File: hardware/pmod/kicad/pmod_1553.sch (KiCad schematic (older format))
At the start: 30 parts, among them IC1 TB001-500-02BE, IC2 TB001-500-02BE, J1 Conn_02x06_Top_Bottom, J2 Conn_01x02, J3 Conn_01x02, P1 78604-9JC, P2 78604-9JC, U2 VO2630, U3 VO2630

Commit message: updated schematic with output filter caps on recieve line. Added AFRL logo as a library so it won't get deleted.
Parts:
- added C5, C6: 10pF, Capacitor_THT:C_Disc_D4.7mm_W2.5mm_P5.00mm, symbol Device:C
- added L1: afrl, logos:afrl, symbol logo:afrl
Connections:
- net GNDD: now also C5.1, C6.2
- net at J1.11 (Pin_11), R9.1, U3.6 (VO2): now also C5.2
- net at J1.9 (Pin_9), R10.2, U3.7 (VO1): now also C6.1
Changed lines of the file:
@@
 	6250 3050 6250 3350
 Connection ~ 6250 3350
+$Comp
+L Device:C C6
+U 1 1 6106DF8C
+P 5050 3600
+F 0 "C6" H 4875 3500 50  0000 L CNN
+F 1 "10pF" H 5100 3500 50  0000 L CNN
+F 2 "Capacitor_THT:C_Disc_D4.7mm_W2.5mm_P5.00mm" H 5088 3450 50  0001 C CNN
+F 3 "~" H 5050 3600 50  0001 C CNN
+	1    5050 3600
+	1    0    0    -1
+$EndComp
+Connection ~ 5050 3450
+$Comp
+L Device:C C5
+U 1 1 6106E50E
+P 4825 2950
+F 0 "C5" H 4625 2950 50  0000 L CNN
+F 1 "10pF" H 4925 2950 50  0000 L CNN
+F 2 "Capacitor_THT:C_Disc_D4.7mm_W2.5mm_P5.00mm" H 4863 2800 50  0001 C CNN
+F 3 "~" H 4825 2950 50  0001 C CNN
+	1    4825 2950
+	0    -1   -1   0
+$EndComp
+Connection ~ 4975 2950
+$Comp
+L power:GNDD #PWR06
+U 1 1 6106F8EA
+P 4675 2950
+F 0 "#PWR06" H 4675 2700 50  0001 C CNN
+F 1 "GNDD" H 4675 2800 50  0000 C CNN
+F 2 "" H 4675 2950 50  0001 C CNN
+F 3 "" H 4675 2950 50  0001 C CNN
+	1    4675 2950
+	0    1    1    0
+$EndComp
+$Comp
+L power:GNDD #PWR08
+U 1 1 6106FFF3
+P 5050 3750
+F 0 "#PWR08" H 5050 3500 50  0001 C CNN
+F 1 "GNDD" H 5050 3600 50  0000 C CNN
+F 2 "" H 5050 3750 50  0001 C CNN
+F 3 "" H 5050 3750 50  0001 C CNN
+	1    5050 3750
+	1    0    0    -1
+$EndComp
+$Comp
+L logo:afrl L1
+U 1 1 6108267E
+P 6050 6125
+F 0 "L1" H 6178 6171 50  0000 L CNN
+F 1 "afrl" H 6178 6080 50  0000 L CNN
+F 2 "logos:afrl" H 6050 6125 50  0001 C CNN
+F 3 "" H 6050 6125 50  0001 C CNN
+	1    6050 6125
+	1    0    0    -1
+$EndComp
 $EndSCHEMATC

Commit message: added testbench for fifos,they are barebones junk, but they are there and work with icarus.
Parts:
- C3, C4: value 22pF -> 10pF
- C5, C6: value 10pF -> 20pF
- R10, R9: value 2K2 -> 2K
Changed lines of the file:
@@
 P 6925 5225
 F 0 "C4" H 6700 5225 50  0000 L CNN
-F 1 "22pF" H 7050 5225 50  0000 L CNN
+F 1 "10pF" H 7050 5225 50  0000 L CNN
 F 2 "Capacitor_THT:C_Disc_D4.7mm_W2.5mm_P5.00mm" H 6963 5075 50  0001 C CNN
 F 3 "~" H 6925 5225 50  0001 C CNN
@@
 P 6925 4525
 F 0 "C3" H 6725 4525 50  0000 L CNN
-F 1 "22pF" H 7025 4525 50  0000 L CNN
+F 1 "10pF" H 7025 4525 50  0000 L CNN
 F 2 "Capacitor_THT:C_Disc_D4.7mm_W2.5mm_P5.00mm" H 6963 4375 50  0001 C CNN
 F 3 "~" H 6925 4525 50  0001 C CNN
@@
 P 5325 3500
 F 0 "R10" V 5118 3500 50  0000 C CNN
-F 1 "2K2" V 5209 3500 50  0000 C CNN
+F 1 "2K" V 5209 3500 50  0000 C CNN
 F 2 "Resistor_THT:R_Axial_DIN0207_L6.3mm_D2.5mm_P7.62mm_Horizontal" V 5255 3500 50  0001 C CNN
 F 3 "~" H 5325 3500 50  0001 C CNN
@@
 P 5325 2800
 F 0 "R9" V 5118 2800 50  0000 C CNN
-F 1 "2K2" V 5209 2800 50  0000 C CNN
+F 1 "2K" V 5209 2800 50  0000 C CNN
 F 2 "Resistor_THT:R_Axial_DIN0207_L6.3mm_D2.5mm_P7.62mm_Horizontal" V 5255 2800 50  0001 C CNN
 F 3 "~" H 5325 2800 50  0001 C CNN
@@
 P 5050 3600
 F 0 "C6" H 4875 3500 50  0000 L CNN
-F 1 "10pF" H 5100 3500 50  0000 L CNN
+F 1 "20pF" H 5100 3500 50  0000 L CNN
 F 2 "Capacitor_THT:C_Disc_D4.7mm_W2.5mm_P5.00mm" H 5088 3450 50  0001 C CNN
 F 3 "~" H 5050 3600 50  0001 C CNN
@@
 P 4825 2950
 F 0 "C5" H 4625 2950 50  0000 L CNN
-F 1 "10pF" H 4925 2950 50  0000 L CNN
+F 1 "20pF" H 4925 2950 50  0000 L CNN
 F 2 "Capacitor_THT:C_Disc_D4.7mm_W2.5mm_P5.00mm" H 4863 2800 50  0001 C CNN
 F 3 "~" H 4825 2950 50  0001 C CNN

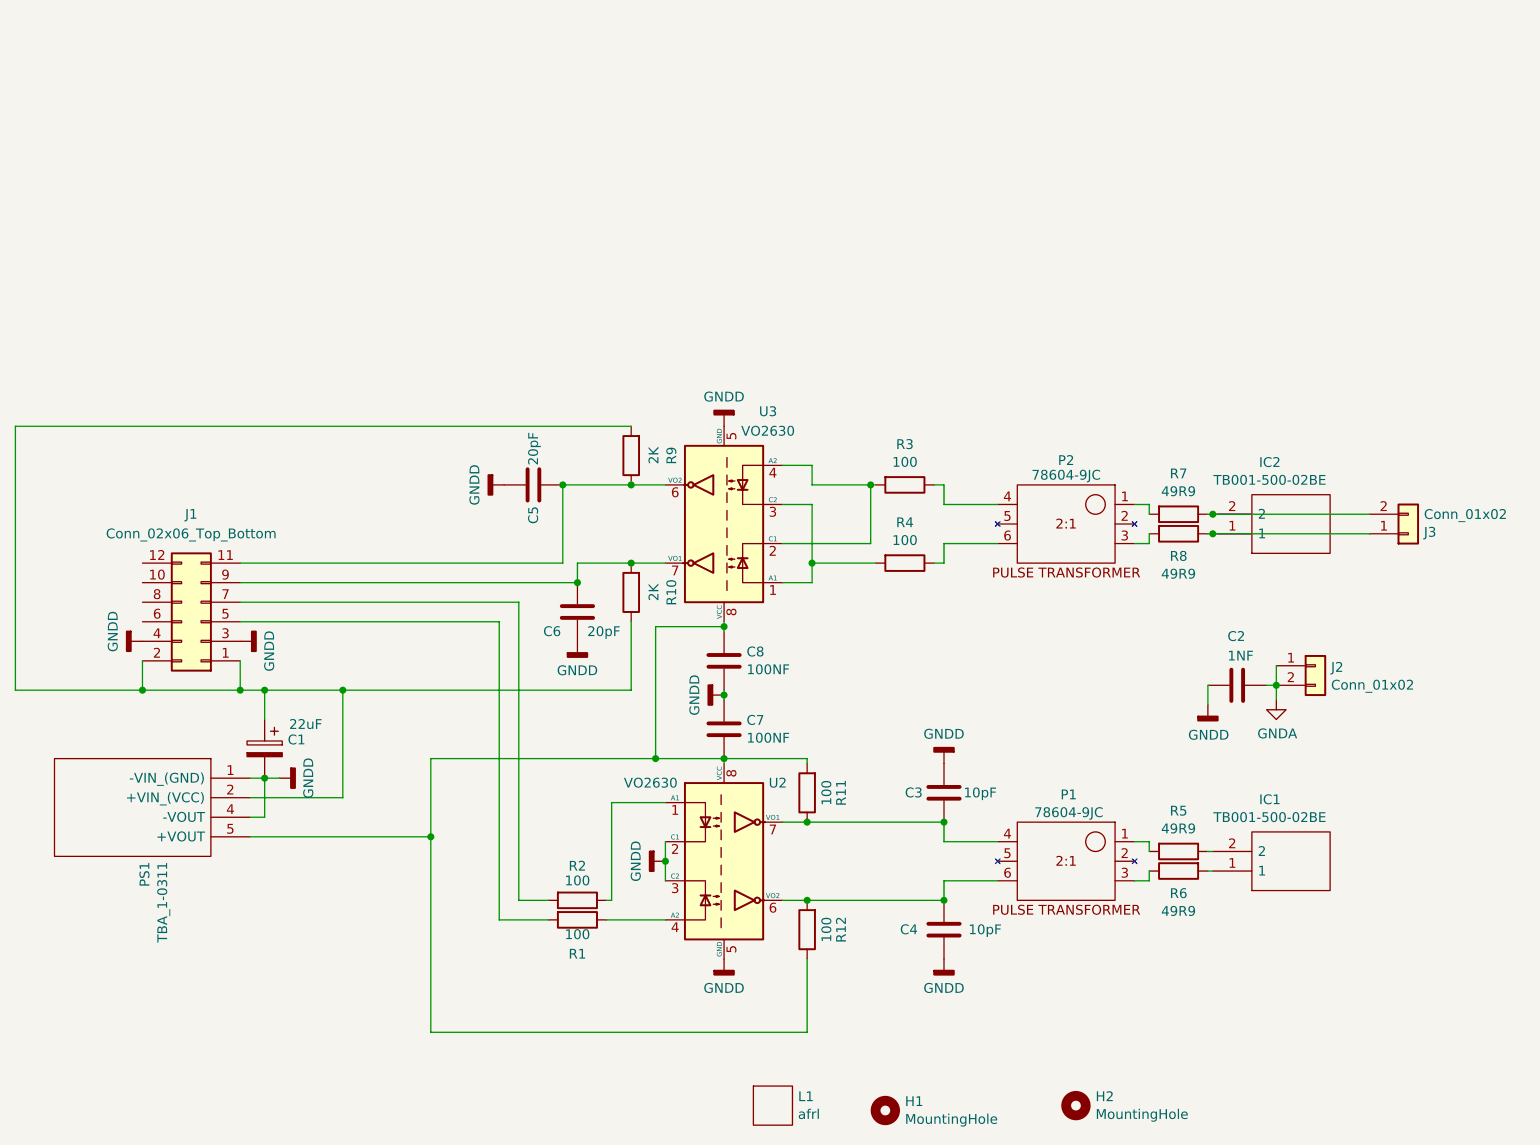
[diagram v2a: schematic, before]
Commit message: added 1553 to fmc1553 core, need adc/dac interface connection. added arty mcs file.
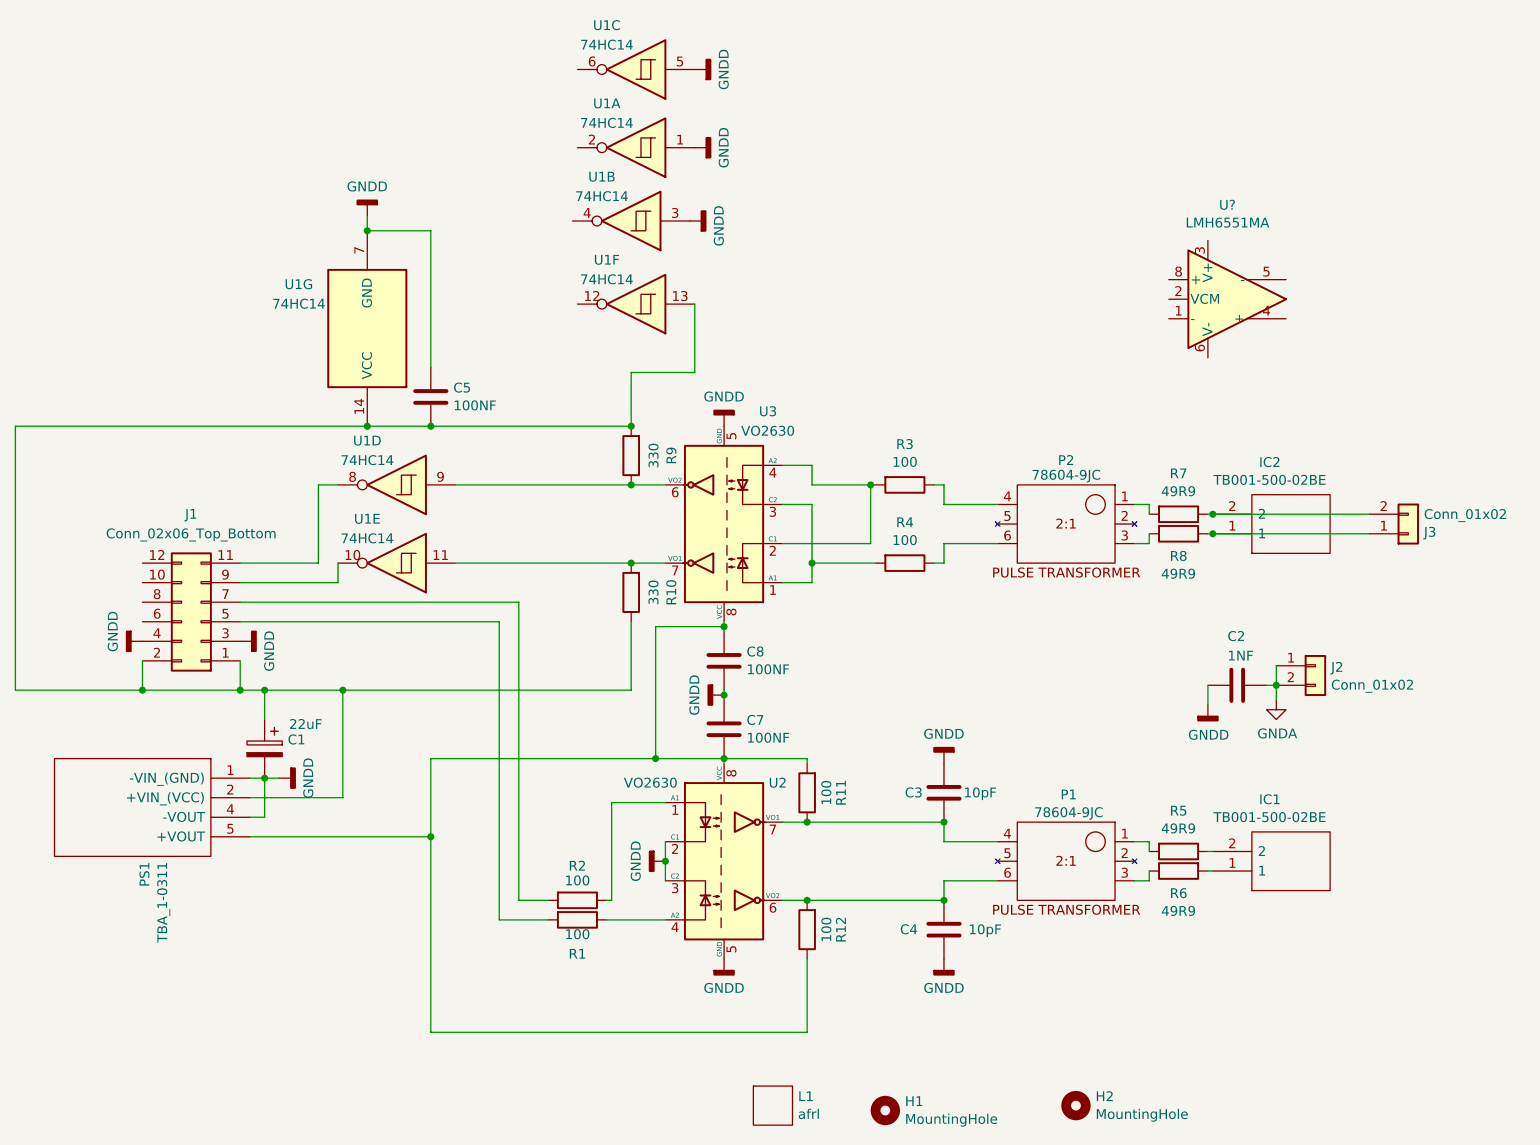
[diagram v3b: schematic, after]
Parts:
- removed C6: 20pF, Capacitor_THT:C_Disc_D4.7mm_W2.5mm_P5.00mm, symbol Device:C
- added U1: 74HC14, Package_DIP:DIP-14_W7.62mm_LongPads, symbol 74xx:74HC14
- added U?: LMH6551MA, Package_SO:SOIC-8_3.9x4.9mm_P1.27mm, symbol Amplifier_Operational:LMH6551MA
- C5: value 20pF -> 100NF
- R10, R9: value 2K -> 330
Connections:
- net GNDD: now also U1.1, U1.3, U1.5, U1.7 (GND)
- net at C1.1, J1.1 (Pin_1), J1.2 (Pin_2)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: now also C5.2, U1.13, U1.14 (VCC)
- net at R9.1, U3.6 (VO2): now also U1.9; no longer C5.2, J1.11 (Pin_11)
- net at R10.2, U3.7 (VO1): now also U1.11; no longer J1.9 (Pin_9)
- new net: J1.11 (Pin_11), U1.8
- new net: J1.9 (Pin_9), U1.10
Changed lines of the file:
@@
 $EndComp
-Wire Wire Line
-	3325 3450 5050 3450
-Wire Wire Line
-	5050 3450 5050 3350
-Wire Wire Line
-	4975 2950 4975 3350
-Wire Wire Line
-	4975 3350 3325 3350
-Wire Wire Line
-	4975 2950 5325 2950
 Wire Wire Line
 	3325 3650 4650 3650
@@
 P 5325 3500
 F 0 "R10" V 5118 3500 50  0000 C CNN
-F 1 "2K" V 5209 3500 50  0000 C CNN
+F 1 "330" V 5209 3500 50  0000 C CNN
 F 2 "Resistor_THT:R_Axial_DIN0207_L6.3mm_D2.5mm_P7.62mm_Horizontal" V 5255 3500 50  0001 C CNN
 F 3 "~" H 5325 3500 50  0001 C CNN
@@
 $EndComp
 Connection ~ 5325 3350
-Wire Wire Line
-	5325 3350 5050 3350
 $Comp
 L Device:R R9
@@
 P 5325 2800
 F 0 "R9" V 5118 2800 50  0000 C CNN
-F 1 "2K" V 5209 2800 50  0000 C CNN
+F 1 "330" V 5209 2800 50  0000 C CNN
 F 2 "Resistor_THT:R_Axial_DIN0207_L6.3mm_D2.5mm_P7.62mm_Horizontal" V 5255 2800 50  0001 C CNN
 F 3 "~" H 5325 2800 50  0001 C CNN
@@
 	2175 4000 2175 2650
 Wire Wire Line
-	2175 2650 5325 2650
+	2175 2650 3975 2650
 Connection ~ 2825 4000
 Wire Wire Line
@@
 Connection ~ 6250 3350
 $Comp
-L Device:C C6
-U 1 1 6106DF8C
-P 5050 3600
-F 0 "C6" H 4875 3500 50  0000 L CNN
-F 1 "20pF" H 5100 3500 50  0000 L CNN
-F 2 "Capacitor_THT:C_Disc_D4.7mm_W2.5mm_P5.00mm" H 5088 3450 50  0001 C CNN
-F 3 "~" H 5050 3600 50  0001 C CNN
-	1    5050 3600
-	1    0    0    -1
-$EndComp
-Connection ~ 5050 3450
-$Comp
-L Device:C C5
-U 1 1 6106E50E
-P 4825 2950
-F 0 "C5" H 4625 2950 50  0000 L CNN
-F 1 "20pF" H 4925 2950 50  0000 L CNN
-F 2 "Capacitor_THT:C_Disc_D4.7mm_W2.5mm_P5.00mm" H 4863 2800 50  0001 C CNN
-F 3 "~" H 4825 2950 50  0001 C CNN
-	1    4825 2950
-	0    -1   -1   0
-$EndComp
-Connection ~ 4975 2950
-$Comp
-L power:GNDD #PWR06
-U 1 1 6106F8EA
-P 4675 2950
-F 0 "#PWR06" H 4675 2700 50  0001 C CNN
-F 1 "GNDD" H 4675 2800 50  0000 C CNN
-F 2 "" H 4675 2950 50  0001 C CNN
-F 3 "" H 4675 2950 50  0001 C CNN
-	1    4675 2950
-	0    1    1    0
-$EndComp
-$Comp
-L power:GNDD #PWR08
-U 1 1 6106FFF3
-P 5050 3750
-F 0 "#PWR08" H 5050 3500 50  0001 C CNN
-F 1 "GNDD" H 5050 3600 50  0000 C CNN
-F 2 "" H 5050 3750 50  0001 C CNN
-F 3 "" H 5050 3750 50  0001 C CNN
-	1    5050 3750
-	1    0    0    -1
-$EndComp
-$Comp
 L logo:afrl L1
 U 1 1 6108267E
@@
 	1    0    0    -1
 $EndComp
+$Comp
+L 74xx:74HC14 U1
+U 1 1 6109BA4C
+P 5350 1225
+F 0 "U1" H 5500 1000 50  0000 C CNN
+F 1 "74HC14" H 5500 1100 50  0000 C CNN
+F 2 "Package_DIP:DIP-14_W7.62mm_LongPads" H 5350 1225 50  0001 C CNN
+F 3 "http://www.ti.com/lit/gpn/sn74HC14" H 5350 1225 50  0001 C CNN
+	1    5350 1225
+	-1   0    0    1
+$EndComp
+$Comp
+L 74xx:74HC14 U1
+U 2 1 610B023C
+P 5325 1600
+F 0 "U1" H 5475 1375 50  0000 C CNN
+F 1 "74HC14" H 5475 1475 50  0000 C CNN
+F 2 "Package_DIP:DIP-14_W7.62mm_LongPads" H 5325 1600 50  0001 C CNN
+F 3 "http://www.ti.com/lit/gpn/sn74HC14" H 5325 1600 50  0001 C CNN
+	2    5325 1600
+	-1   0    0    1
+$EndComp
+Wire Wire Line
+	4425 2950 5325 2950
+Wire Wire Line
+	4425 3350 5325 3350
+Wire Wire Line
+	3825 3450 3325 3450
+Wire Wire Line
+	3325 3350 3725 3350
+Wire Wire Line
+	3725 3350 3725 2950
+Wire Wire Line
+	3725 2950 3825 2950
+Wire Wire Line
+	3825 3350 3825 3450
+$Comp
+L 74xx:74HC14 U1
+U 7 1 610D764E
+P 3975 2150
+F 0 "U1" H 4325 1925 50  0000 C CNN
+F 1 "74HC14" H 4325 2025 50  0000 C CNN
+F 2 "Package_DIP:DIP-14_W7.62mm_LongPads" H 3975 2150 50  0001 C CNN
+F 3 "http://www.ti.com/lit/gpn/sn74HC14" H 3975 2150 50  0001 C CNN
+	7    3975 2150
+	-1   0    0    1
+$EndComp
+Connection ~ 3975 2650
+$Comp
+L power:GNDD #PWR06
+U 1 1 610E20D2
+P 3975 1575
+F 0 "#PWR06" H 3975 1325 50  0001 C CNN
+F 1 "GNDD" H 3975 1425 50  0000 C CNN
+F 2 "" H 3975 1575 50  0001 C CNN
+F 3 "" H 3975 1575 50  0001 C CNN
+	1    3975 1575
+	-1   0    0    1
+$EndComp
+$Comp
+L Device:C C5
+U 1 1 610E2A33
+P 4300 2500
+F 0 "C5" H 4415 2546 50  0000 L CNN
+F 1 "100NF" H 4415 2455 50  0000 L CNN
+F 2 "Capacitor_THT:C_Disc_D4.7mm_W2.5mm_P5.00mm" H 4338 2350 50  0001 C CNN
+F 3 "~" H 4300 2500 50  0001 C CNN
+	1    4300 2500
+	1    0    0    -1
+$EndComp
+Wire Wire Line
+	3975 1650 3975 1575
+Connection ~ 3975 1650
+Connection ~ 4300 2650
+Wire Wire Line
+	4300 2650 5325 2650
+Wire Wire Line
+	3975 2650 4300 2650
+Wire Wire Line
+	4300 2350 4300 1650
+Wire Wire Line
+	3975 1650 4300 1650
+$Comp
+L 74xx:74HC14 U1
+U 5 1 61103622
+P 4125 3350
+F 0 "U1" H 4275 3125 50  0000 C CNN
+F 1 "74HC14" H 4275 3225 50  0000 C CNN
+F 2 "" H 4125 3350 50  0001 C CNN
+F 3 "http://www.ti.com/lit/gpn/sn74HC14" H 4125 3350 50  0001 C CNN
+	5    4125 3350
+	-1   0    0    1
+$EndComp
+$Comp
+L 74xx:74HC14 U1
+U 6 1 61106EEA
+P 5350 2025
+F 0 "U1" H 5500 1800 50  0000 C CNN
+F 1 "74HC14" H 5500 1900 50  0000 C CNN
+F 2 "" H 5350 2025 50  0001 C CNN
+F 3 "http://www.ti.com/lit/gpn/sn74HC14" H 5350 2025 50  0001 C CNN
+	6    5350 2025
+	-1   0    0    1
+$EndComp
+$Comp
+L 74xx:74HC14 U1
+U 4 1 6110A8C5
+P 4125 2950
+F 0 "U1" H 4275 2725 50  0000 C CNN
+F 1 "74HC14" H 4275 2825 50  0000 C CNN
+F 2 "" H 4125 2950 50  0001 C CNN
+F 3 "http://www.ti.com/lit/gpn/sn74HC14" H 4125 2950 50  0001 C CNN
+	4    4125 2950
+	-1   0    0    1
+$EndComp
+$Comp
+L 74xx:74HC14 U1
+U 3 1 6110E653
+P 5350 825
+F 0 "U1" H 5500 600 50  0000 C CNN
+F 1 "74HC14" H 5500 700 50  0000 C CNN
+F 2 "" H 5350 825 50  0001 C CNN
+F 3 "http://www.ti.com/lit/gpn/sn74HC14" H 5350 825 50  0001 C CNN
+	3    5350 825
+	-1   0    0    1
+$EndComp
+$Comp
+L power:GNDD #PWR0105
+U 1 1 6111725A
+P 5625 1600
+F 0 "#PWR0105" H 5625 1350 50  0001 C CNN
+F 1 "GNDD" H 5600 1450 50  0000 C CNN
+F 2 "" H 5625 1600 50  0001 C CNN
+F 3 "" H 5625 1600 50  0001 C CNN
+	1    5625 1600
+	0    -1   -1   0
+$EndComp
+$Comp
+L power:GNDD #PWR0106
+U 1 1 6111F143
+P 5650 1225
+F 0 "#PWR0106" H 5650 975 50  0001 C CNN
+F 1 "GNDD" H 5650 1075 50  0000 C CNN
+F 2 "" H 5650 1225 50  0001 C CNN
+F 3 "" H 5650 1225 50  0001 C CNN
+	1    5650 1225
+	0    -1   -1   0
+$EndComp
+$Comp
+L power:GNDD #PWR0107
+U 1 1 61124E1C
+P 5650 825
+F 0 "#PWR0107" H 5650 575 50  0001 C CNN
+F 1 "GNDD" H 5650 675 50  0000 C CNN
+F 2 "" H 5650 825 50  0001 C CNN
+F 3 "" H 5650 825 50  0001 C CNN
+	1    5650 825
+	0    -1   -1   0
+$EndComp
+Wire Wire Line
+	5325 2650 5325 2375
+Wire Wire Line
+	5325 2375 5650 2375
+Wire Wire Line
+	5650 2375 5650 2025
+Connection ~ 5325 2650
+$Comp
+L Amplifier_Operational:LMH6551MA U?
+U 1 1 610B4B6E
+P 8375 2000
+F 0 "U?" H 8375 2481 50  0000 C CNN
+F 1 "LMH6551MA" H 8375 2390 50  0000 C CNN
+F 2 "Package_SO:SOIC-8_3.9x4.9mm_P1.27mm" H 8475 1400 50  0001 C CNN
+F 3 "http://www.ti.com/lit/ds/symlink/lmh6551.pdf" H 9375 1700 50  0001 C CNN
+	1    8375 2000
+	1    0    0    -1
+$EndComp

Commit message: added documents for linux build, dac switch added, and pcb has small updates.
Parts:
- removed U?: LMH6551MA, Package_SO:SOIC-8_3.9x4.9mm_P1.27mm, symbol Amplifier_Operational:LMH6551MA
- added C6, C9: 22pF_DNP, Capacitor_THT:C_Disc_D4.7mm_W2.5mm_P5.00mm, symbol Device:C
- R10, R9: value 330 -> 330_2K2-DNP
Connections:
- net GNDD: now also C6.2, C9.2
- net at R9.1, U1.9, U3.6 (VO2): now also C6.1
- net at R10.2, U1.11, U3.7 (VO1): now also C9.1
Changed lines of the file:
@@
 P 5325 3500
 F 0 "R10" V 5118 3500 50  0000 C CNN
-F 1 "330" V 5209 3500 50  0000 C CNN
+F 1 "330_2K2-DNP" V 5209 3500 50  0000 C CNN
 F 2 "Resistor_THT:R_Axial_DIN0207_L6.3mm_D2.5mm_P7.62mm_Horizontal" V 5255 3500 50  0001 C CNN
 F 3 "~" H 5325 3500 50  0001 C CNN
@@
 P 5325 2800
 F 0 "R9" V 5118 2800 50  0000 C CNN
-F 1 "330" V 5209 2800 50  0000 C CNN
+F 1 "330_2K2-DNP" V 5209 2800 50  0000 C CNN
 F 2 "Resistor_THT:R_Axial_DIN0207_L6.3mm_D2.5mm_P7.62mm_Horizontal" V 5255 2800 50  0001 C CNN
 F 3 "~" H 5325 2800 50  0001 C CNN
@@
 $EndComp
 Wire Wire Line
-	4425 2950 5325 2950
-Wire Wire Line
-	4425 3350 5325 3350
+	4425 2950 4750 2950
+Wire Wire Line
+	4425 3350 5000 3350
 Wire Wire Line
 	3825 3450 3325 3450
@@
 Connection ~ 5325 2650
 $Comp
-L Amplifier_Operational:LMH6551MA U?
-U 1 1 610B4B6E
-P 8375 2000
-F 0 "U?" H 8375 2481 50  0000 C CNN
-F 1 "LMH6551MA" H 8375 2390 50  0000 C CNN
-F 2 "Package_SO:SOIC-8_3.9x4.9mm_P1.27mm" H 8475 1400 50  0001 C CNN
-F 3 "http://www.ti.com/lit/ds/symlink/lmh6551.pdf" H 9375 1700 50  0001 C CNN
-	1    8375 2000
-	1    0    0    -1
-$EndComp
+L Device:C C9
+U 1 1 610CA7A8
+P 5000 3500
+F 0 "C9" H 4800 3500 50  0000 L CNN
+F 1 "22pF_DNP" H 4850 3400 50  0000 L CNN
+F 2 "Capacitor_THT:C_Disc_D4.7mm_W2.5mm_P5.00mm" H 5038 3350 50  0001 C CNN
+F 3 "~" H 5000 3500 50  0001 C CNN
+	1    5000 3500
+	1    0    0    -1
+$EndComp
+Connection ~ 5000 3350
+Wire Wire Line
+	5000 3350 5325 3350
+$Comp
+L Device:C C6
+U 1 1 610CB109
+P 4750 3100
+F 0 "C6" H 4625 3000 50  0000 L CNN
+F 1 "22pF_DNP" H 4875 3100 50  0000 L CNN
+F 2 "Capacitor_THT:C_Disc_D4.7mm_W2.5mm_P5.00mm" H 4788 2950 50  0001 C CNN
+F 3 "~" H 4750 3100 50  0001 C CNN
+	1    4750 3100
+	1    0    0    -1
+$EndComp
+Connection ~ 4750 2950
+Wire Wire Line
+	4750 2950 5325 2950
+$Comp
+L power:GNDD #PWR08
+U 1 1 610CC809
+P 4750 3250
+F 0 "#PWR08" H 4750 3000 50  0001 C CNN
+F 1 "GNDD" H 4750 3100 50  0000 C CNN
+F 2 "" H 4750 3250 50  0001 C CNN
+F 3 "" H 4750 3250 50  0001 C CNN
+	1    4750 3250
+	1    0    0    -1
+$EndComp
+$Comp
+L power:GNDD #PWR011
+U 1 1 610CD1AE
+P 5000 3650
+F 0 "#PWR011" H 5000 3400 50  0001 C CNN
+F 1 "GNDD" H 5000 3500 50  0000 C CNN
+F 2 "" H 5000 3650 50  0001 C CNN
+F 3 "" H 5000 3650 50  0001 C CNN
+	1    5000 3650
+	1    0    0    -1
+$EndComp
